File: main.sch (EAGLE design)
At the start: 29 parts, among them IC1 SN754410, IC2 7805T, T1 BPX81, T2 BPX81, T3 BPX81, T4 BPX81

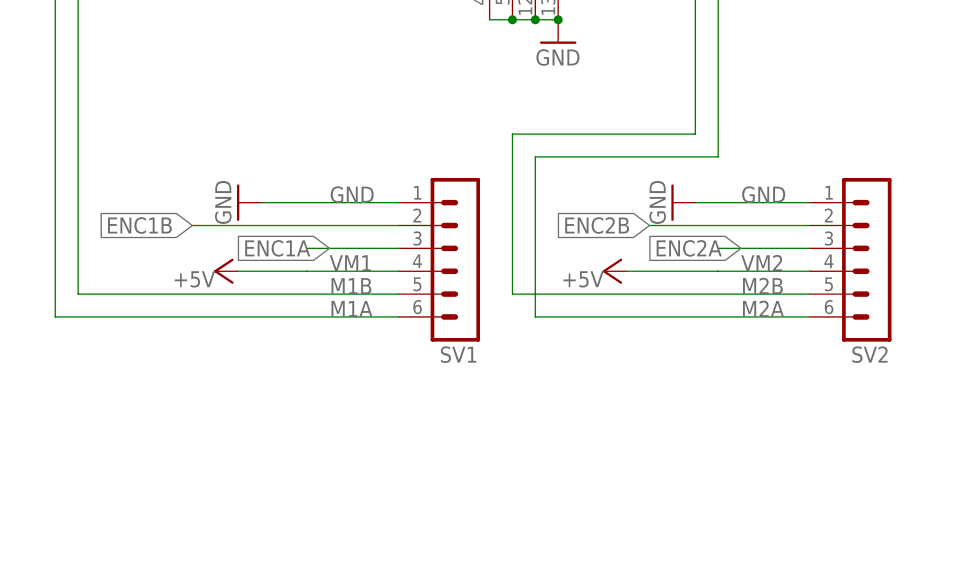
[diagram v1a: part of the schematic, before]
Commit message: Fixed broken nets on motor connectors
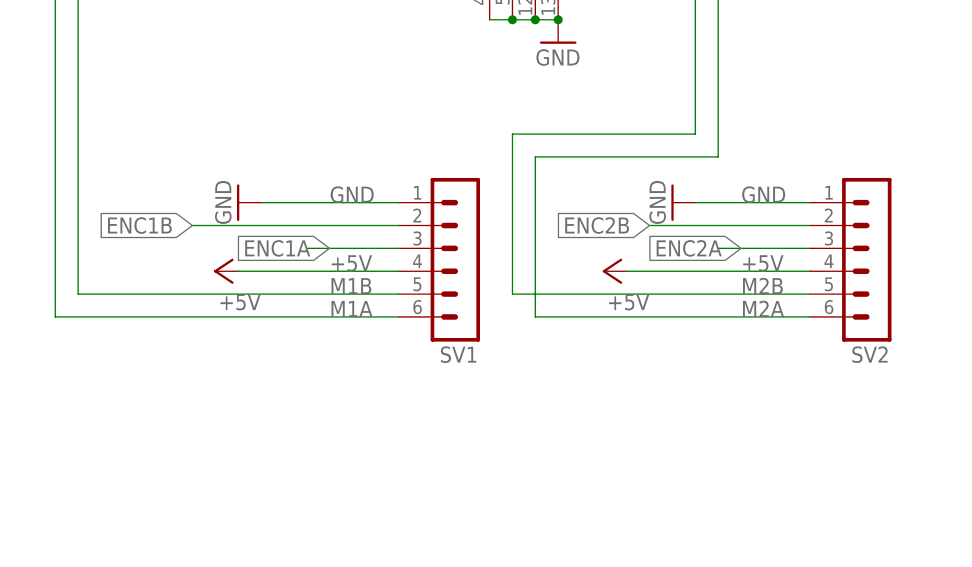
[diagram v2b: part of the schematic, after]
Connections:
- removed net VM1: SV1.4
- removed net VM2: SV2.4
- net +5V: now also SV1.4, SV2.4
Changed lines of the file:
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@@
 <part name="P+5" library="supply1" library_urn="urn:adsk.eagle:library:371" deviceset="+5V" device=""/>
 <part name="TEENSY" library="teensy" deviceset="TEENSY" device=""/>
-<part name="P+2" library="supply1" library_urn="urn:adsk.eagle:library:371" deviceset="+5V" device=""/>
-<part name="P+6" library="supply1" library_urn="urn:adsk.eagle:library:371" deviceset="+5V" device=""/>
 <part name="SV1" library="con-lstb" library_urn="urn:adsk.eagle:library:162" deviceset="MA06-1" device="" package3d_urn="urn:adsk.eagle:package:8340/1"/>
 <part name="SV2" library="con-lstb" library_urn="urn:adsk.eagle:library:162" deviceset="MA06-1" device="" package3d_urn="urn:adsk.eagle:package:8340/1"/>
@@
 <part name="U$2" library="personal" deviceset="POLULUMOTOR" device=""/>
 <part name="U$1" library="personal" deviceset="POLULUMOTOR" device=""/>
+<part name="P+1" library="supply1" library_urn="urn:adsk.eagle:library:371" deviceset="+5V" device=""/>
+<part name="P+2" library="supply1" library_urn="urn:adsk.eagle:library:371" deviceset="+5V" device=""/>
 </parts>
 <sheets>
@@
 <attribute name="VALUE" x="71.12" y="104.14" size="1.778" layer="96" rot="R270"/>
 </instance>
-<instance part="P+2" gate="1" x="170.18" y="71.12" smashed="yes" rot="R90">
-<attribute name="VALUE" x="170.18" y="71.12" size="1.778" layer="96" rot="R180"/>
-</instance>
-<instance part="P+6" gate="1" x="213.36" y="71.12" smashed="yes" rot="R90">
-<attribute name="VALUE" x="213.36" y="71.12" size="1.778" layer="96" rot="R180"/>
-</instance>
 <instance part="SV1" gate="1" x="198.12" y="71.12" smashed="yes" rot="R180">
 <attribute name="VALUE" x="199.39" y="83.82" size="1.778" layer="96" rot="R180"/>
@@
 <instance part="U$2" gate="G$1" x="12.7" y="10.16" smashed="yes"/>
 <instance part="U$1" gate="G$1" x="12.7" y="15.24" smashed="yes"/>
+<instance part="P+1" gate="1" x="170.18" y="71.12" smashed="yes" rot="R90">
+<attribute name="VALUE" x="175.26" y="68.58" size="1.778" layer="96" rot="R180"/>
+</instance>
+<instance part="P+2" gate="1" x="213.36" y="71.12" smashed="yes" rot="R90">
+<attribute name="VALUE" x="218.44" y="68.58" size="1.778" layer="96" rot="R180"/>
+</instance>
 </instances>
 <busses>
@@
 <wire x1="73.66" y1="165.1" x2="78.74" y2="165.1" width="0.1524" layer="91"/>
 </segment>
+<segment>
+<pinref part="SV1" gate="1" pin="4"/>
+<wire x1="190.5" y1="71.12" x2="172.72" y2="71.12" width="0.1524" layer="91"/>
+<label x="182.88" y="71.12" size="1.778" layer="95"/>
+<pinref part="P+1" gate="1" pin="+5V"/>
+</segment>
+<segment>
+<pinref part="SV2" gate="1" pin="4"/>
+<label x="228.6" y="71.12" size="1.778" layer="95"/>
+<wire x1="236.22" y1="71.12" x2="215.9" y2="71.12" width="0.1524" layer="91"/>
+<pinref part="P+2" gate="1" pin="+5V"/>
+</segment>
 </net>
 <net name="N$9" class="0">
@@
 <wire x1="154.94" y1="109.22" x2="154.94" y2="68.58" width="0.1524" layer="91"/>
 <wire x1="154.94" y1="68.58" x2="190.5" y2="68.58" width="0.1524" layer="91"/>
-</segment>
-</net>
-<net name="VM1" class="0">
-<segment>
-<pinref part="SV1" gate="1" pin="4"/>
-<wire x1="190.5" y1="71.12" x2="180.34" y2="71.12" width="0.1524" layer="91"/>
-<label x="182.88" y="71.12" size="1.778" layer="95"/>
-<pinref part="P+2" gate="1" pin="+5V"/>
-<wire x1="180.34" y1="71.12" x2="172.72" y2="71.12" width="0.1524" layer="91"/>
 </segment>
 </net>
@@
 </segment>
 </net>
-<net name="VM2" class="0">
-<segment>
-<pinref part="SV2" gate="1" pin="4"/>
-<wire x1="236.22" y1="71.12" x2="226.06" y2="71.12" width="0.1524" layer="91"/>
-<label x="228.6" y="71.12" size="1.778" layer="95"/>
-<pinref part="P+6" gate="1" pin="+5V"/>
-<wire x1="226.06" y1="71.12" x2="215.9" y2="71.12" width="0.1524" layer="91"/>
-</segment>
-</net>
